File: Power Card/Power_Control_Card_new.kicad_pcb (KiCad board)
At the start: 2 copper layers, 100 x 62.5 mm, 25 parts, among them J4 Conn_01x04_Pin, Q1 IRF5305PbF, Q2 IRF5305PbF, U3 TSR2-2450, U4 TSR2-2433, U5 MCP9808_MSOP

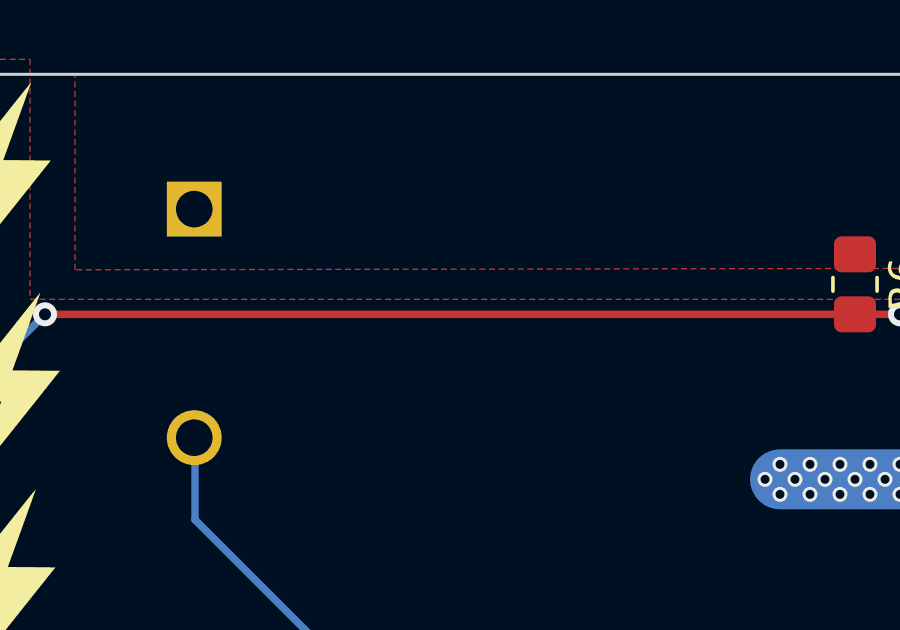
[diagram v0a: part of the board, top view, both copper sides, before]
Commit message: 2nd Kill switch short and fixed connections
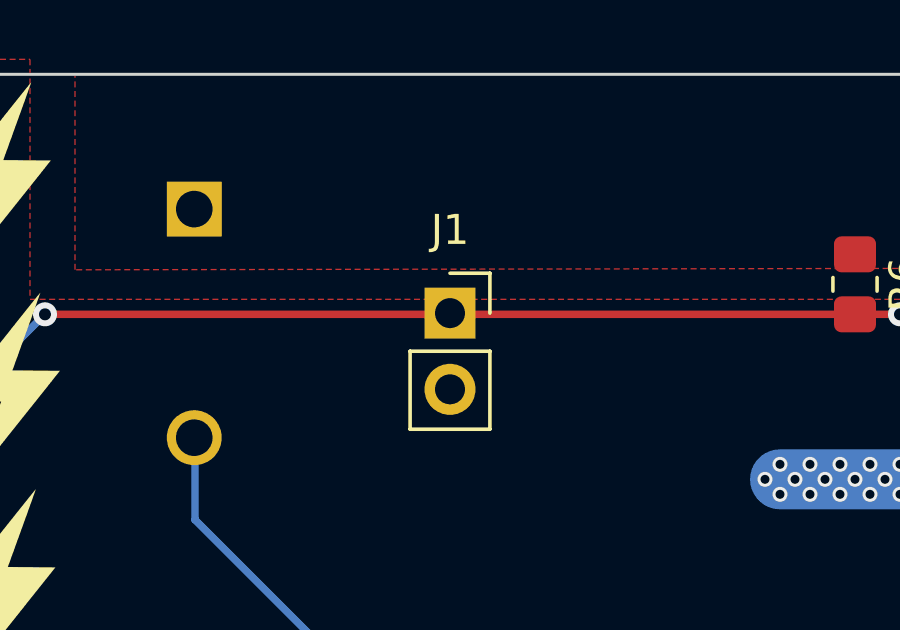
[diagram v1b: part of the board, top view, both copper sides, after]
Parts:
- added J1: Conn_01x02_Pin, Connector_PinSocket_2.54mm:PinSocket_1x02_P2.54mm_Vertical, F.Cu at (216.5, 57.0)
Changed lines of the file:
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@@
 		(embedded_fonts no)
+	)
+	(footprint "Connector_PinSocket_2.54mm:PinSocket_1x02_P2.54mm_Vertical"
+		(layer "F.Cu")
+		(at 216.5 56.96)
+		(descr "Through hole straight socket strip, 1x02, 2.54mm pitch, single row (from Kicad 4.0.7), script generated")
+		(tags "Through hole socket strip THT 1x02 2.54mm single row")
+		(property "Reference" "J1"
+			(at 0 -2.77 0)
+			(layer "F.SilkS")
+			(effects
+				(font
+					(size 1 1)
+					(thickness 0.15)
+				)
+			)
+		)
+		(property "Value" "Conn_01x02_Pin"
+			(at 0 5.31 0)
+			(layer "F.Fab")
+			(effects
+				(font
+					(size 1 1)
+					(thickness 0.15)
+				)
+			)
+		)
+		(property "Datasheet" "~"
+			(at 0 0 0)
+			(layer "F.Fab")
+			(hide yes)
+			(effects
+				(font
+					(size 1.27 1.27)
+					(thickness 0.15)
+				)
+			)
+		)
+		(property "Description" "Generic connector, single row, 01x02, script generated"
+			(at 0 0 0)
+			(layer "F.Fab")
+			(hide yes)
+			(effects
+				(font
+					(size 1.27 1.27)
+					(thickness 0.15)
+				)
+			)
+		)
+		(property ki_fp_filters "Connector*:*_1x??_*")
+		(sheetname "/")
+		(sheetfile "Power_Control_Card_new.kicad_sch")
+		(attr through_hole)
+		(fp_line
+			(start -1.33 1.27)
+			(end -1.33 3.87)
+			(stroke
+				(width 0.12)
+				(type solid)
+			)
+			(layer "F.SilkS")
+		)
+		(fp_line
+			(start -1.33 1.27)
+			(end 1.33 1.27)
+			(stroke
+				(width 0.12)
+				(type solid)
+			)
+			(layer "F.SilkS")
+		)
+		(fp_line
+			(start -1.33 3.87)
+			(end 1.33 3.87)
+			(stroke
+				(width 0.12)
+				(type solid)
+			)
+			(layer "F.SilkS")
+		)
+		(fp_line
+			(start 0 -1.33)
+			(end 1.33 -1.33)
+			(stroke
+				(width 0.12)
+				(type solid)
+			)
+			(layer "F.SilkS")
+		)
+		(fp_line
+			(start 1.33 -1.33)
+			(end 1.33 0)
+			(stroke
+				(width 0.12)
+				(type solid)
+			)
+			(layer "F.SilkS")
+		)
+		(fp_line
+			(start 1.33 1.27)
+			(end 1.33 3.87)
+			(stroke
+				(width 0.12)
+				(type solid)
+			)
+			(layer "F.SilkS")
+		)
+		(fp_line
+			(start -1.8 -1.8)
+			(end 1.75 -1.8)
+			(stroke
+				(width 0.05)
+				(type solid)
+			)
+			(layer "F.CrtYd")
+		)
+		(fp_line
+			(start -1.8 4.3)
+			(end -1.8 -1.8)
+			(stroke
+				(width 0.05)
+				(type solid)
+			)
+			(layer "F.CrtYd")
+		)
+		(fp_line
+			(start 1.75 -1.8)
+			(end 1.75 4.3)
+			(stroke
+				(width 0.05)
+				(type solid)
+			)
+			(layer "F.CrtYd")
+		)
+		(fp_line
+			(start 1.75 4.3)
+			(end -1.8 4.3)
+			(stroke
+				(width 0.05)
+				(type solid)
+			)
+			(layer "F.CrtYd")
+		)
+		(fp_line
+			(start -1.27 -1.27)
+			(end 0.635 -1.27)
+			(stroke
+				(width 0.1)
+				(type solid)
+			)
+			(layer "F.Fab")
+		)
+		(fp_line
+			(start -1.27 3.81)
+			(end -1.27 -1.27)
+			(stroke
+				(width 0.1)
+				(type solid)
+			)
+			(layer "F.Fab")
+		)
+		(fp_line
+			(start 0.635 -1.27)
+			(end 1.27 -0.635)
+			(stroke
+				(width 0.1)
+				(type solid)
+			)
+			(layer "F.Fab")
+		)
+		(fp_line
+			(start 1.27 -0.635)
+			(end 1.27 3.81)
+			(stroke
+				(width 0.1)
+				(type solid)
+			)
+			(layer "F.Fab")
+		)
+		(fp_line
+			(start 1.27 3.81)
+			(end -1.27 3.81)
+			(stroke
+				(width 0.1)
+				(type solid)
+			)
+			(layer "F.Fab")
+		)
+		(fp_text user "${REFERENCE}"
+			(at 0 1.27 90)
+			(layer "F.Fab")
+			(effects
+				(font
+					(size 1 1)
+					(thickness 0.15)
+				)
+			)
+		)
+		(pad "1" thru_hole rect
+			(at 0 0)
+			(size 1.7 1.7)
+			(drill 1)
+			(layers "*.Cu" "*.Mask")
+			(remove_unused_layers no)
+			(net 33 "NJSW1")
+			(pinfunction "Pin_1")
+			(pintype "passive")
+		)
+		(pad "2" thru_hole circle
+			(at 0 2.54)
+			(size 1.7 1.7)
+			(drill 1)
+			(layers "*.Cu" "*.Mask")
+			(remove_unused_layers no)
+			(net 35 "GND")
+			(pinfunction "Pin_2")
+			(pintype "passive")
+		)
+		(embedded_fonts no)
+		(model "${KICAD9_3DMODEL_DIR}/Connector_PinSocket_2.54mm.3dshapes/PinSocket_1x02_P2.54mm_Vertical.step"
+			(offset
+				(xyz 0 0 0)
+			)
+			(scale
+				(xyz 1 1 1)
+			)
+			(rotate
+				(xyz 0 0 0)
+			)
+		)
 	)
 	(footprint "Package_TO_SOT_THT:TO-220-3_Vertical"
